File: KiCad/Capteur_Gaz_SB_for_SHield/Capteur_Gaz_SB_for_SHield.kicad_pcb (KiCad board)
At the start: 2 copper layers, 53.3 x 47 mm, 18 parts, among them J1 Conn_01x02_Female, J2 Conn_01x04_Male, Q1 IRF540N, U1 Capteur_TO-5, U2 LTC1050

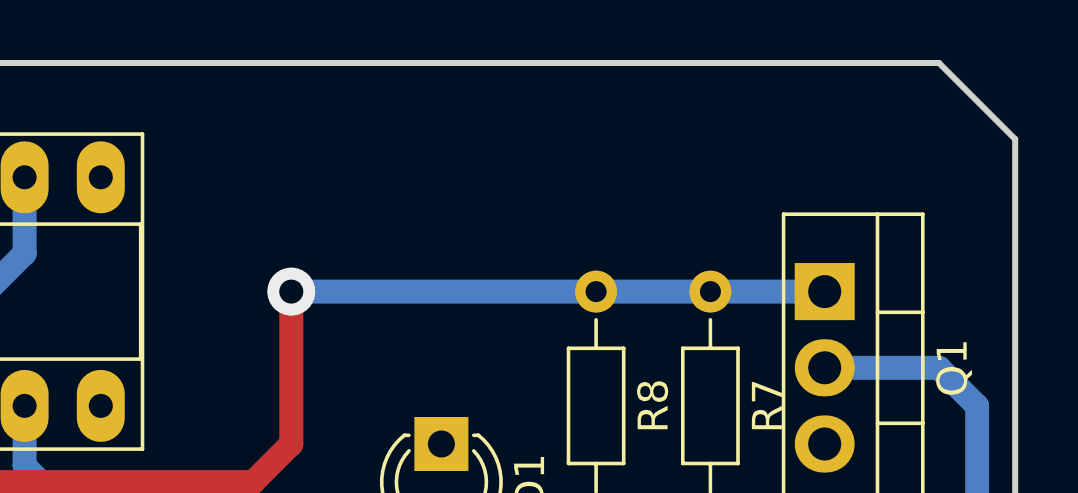
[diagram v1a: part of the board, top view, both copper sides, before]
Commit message: Ajout du text sur les pcbs
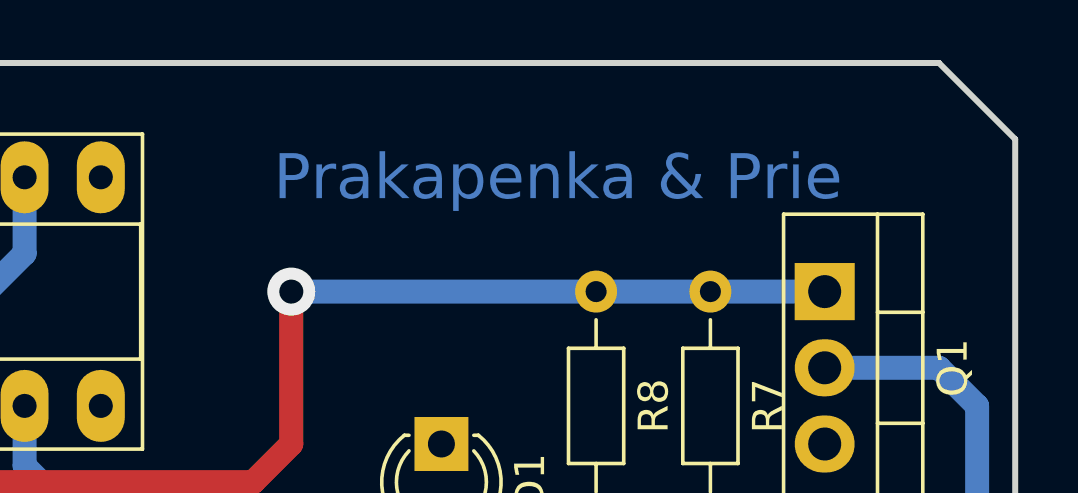
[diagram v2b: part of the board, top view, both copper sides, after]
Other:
- board text added: "Prakapenka & Prie"
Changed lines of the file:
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@@
   (general
     (thickness 1.6)
-    (drawings 8)
+    (drawings 9)
     (tracks 75)
     (zones 0)
@@
     )
   )
+  (gr_text "Prakapenka & Prie" (at 137.16 45.72) (layer B.Cu)
+    (effects (font (size 1.5 1.5) (thickness 0.3)))
+  )
   (gr_line (start 149.86 41.91) (end 101.6 41.91) (layer Edge.Cuts) (width 0.2))
